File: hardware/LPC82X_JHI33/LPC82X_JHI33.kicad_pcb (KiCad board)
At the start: 2 copper layers, 23.6 x 23.5 mm, 24 parts, among them J1 Conn_02x09_Odd_Even, J2 Conn_02x09_Odd_Even, J3 JTAG_2X05, U1 LPC824M201JHI33, Y1 12MHz

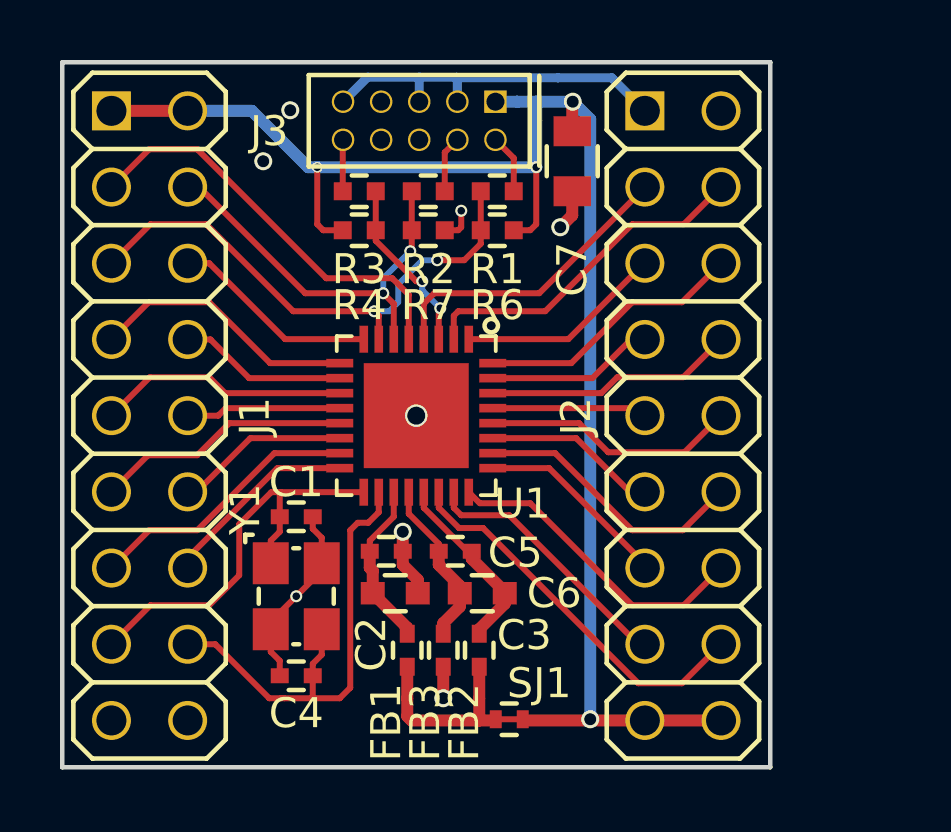
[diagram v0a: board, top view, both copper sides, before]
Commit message: LPC824 QFN33 new footprint for LPC and shrunk paste size
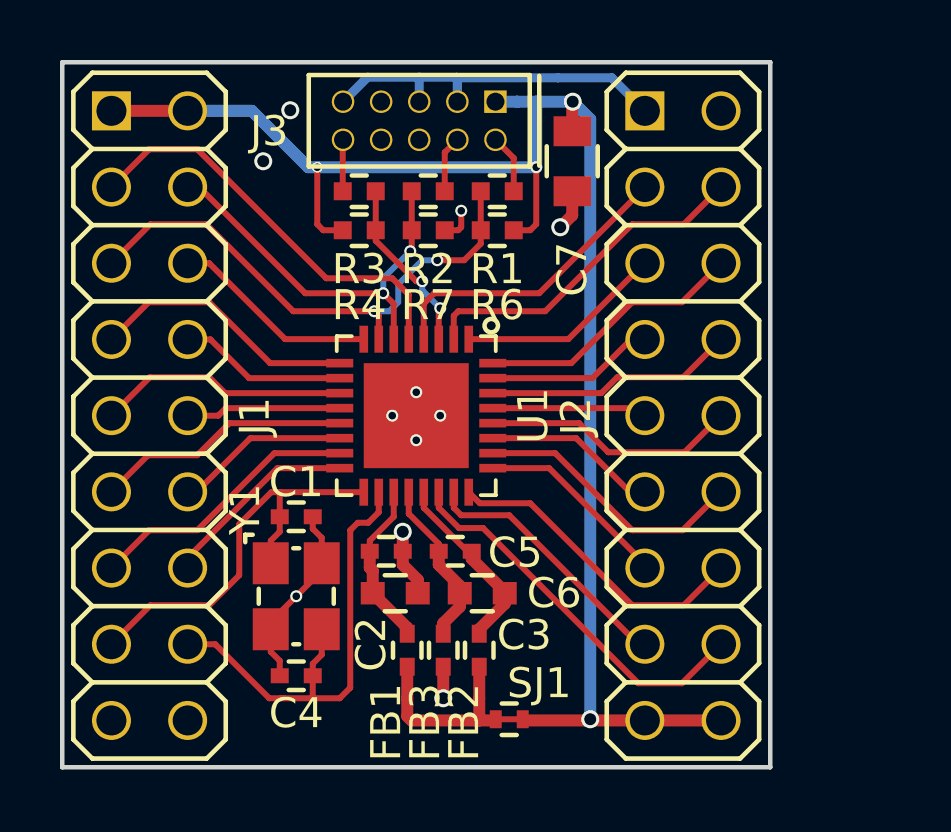
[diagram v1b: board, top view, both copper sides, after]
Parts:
- N2: value 20181124 -> 20190313
- U1: footprint SquantorIC:SOT617-3 -> SquantorIC:SOT617-3_alt_paste
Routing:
- net VSS: vias 8 -> 11
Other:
- rule solder_mask_min_width: 0.2 -> 0.1

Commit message: pcb net updates
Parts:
- N2: value 20190313 -> 20190411
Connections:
- net VDD renamed /VDD
- net VSS renamed /VSS

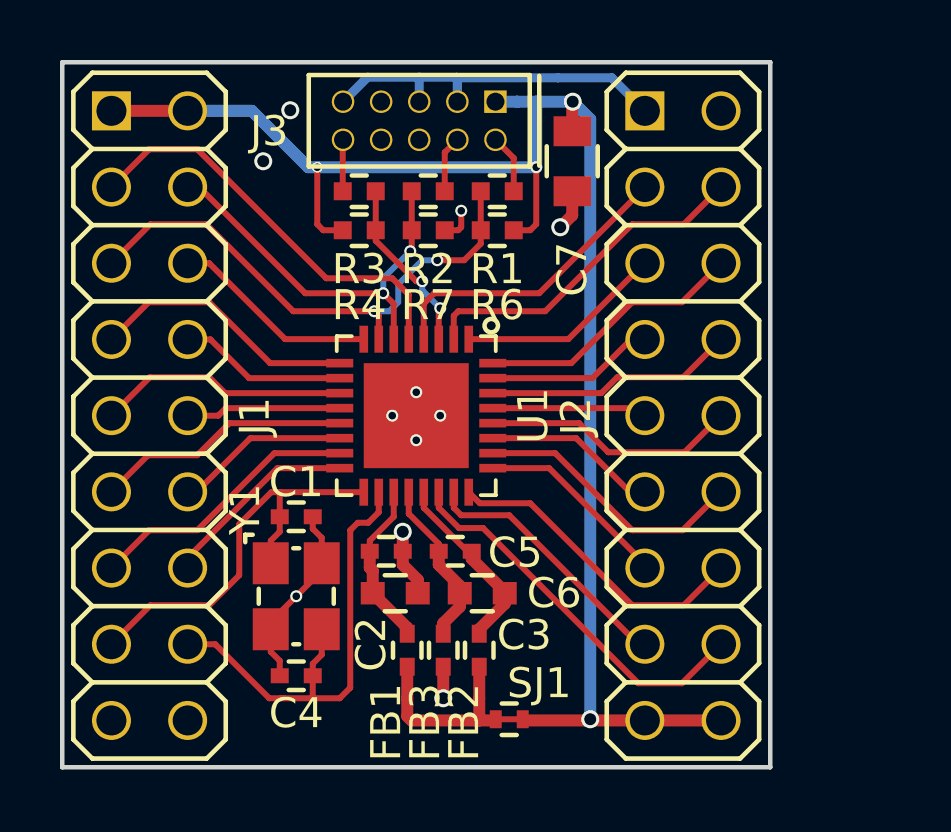
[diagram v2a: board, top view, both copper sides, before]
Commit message: changed connectors, newer component library
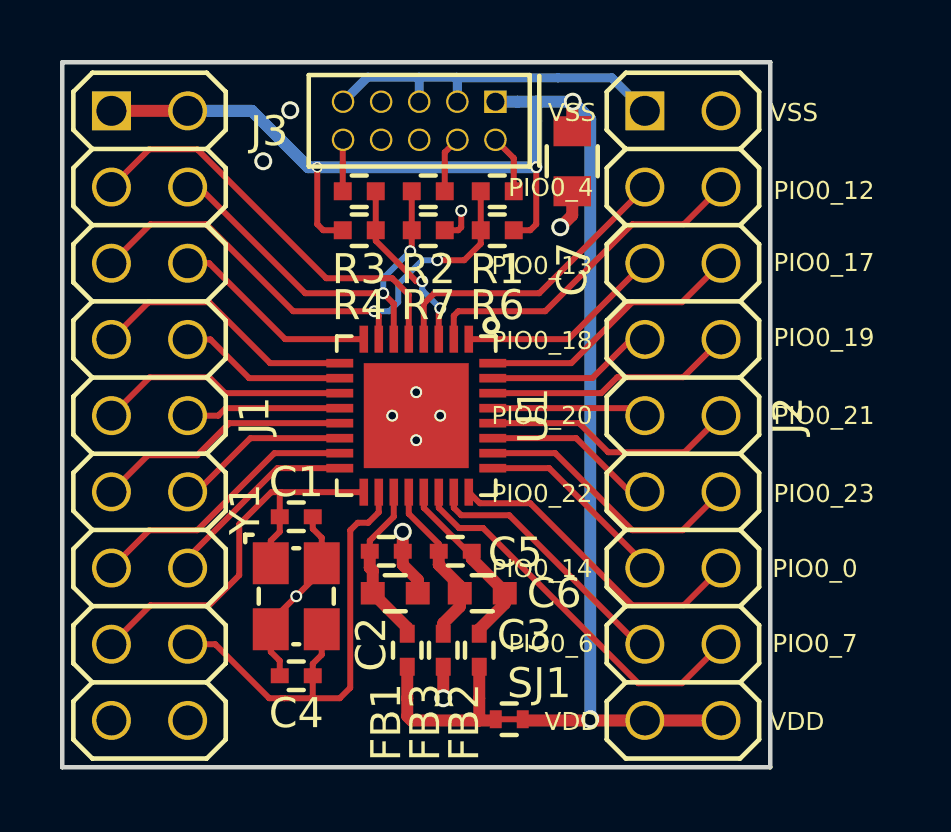
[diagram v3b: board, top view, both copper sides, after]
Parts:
- J1: value Conn_02x09_Odd_Even -> LPC82XJHI33_LEFT; footprint SquantorConnectors:Header-0254-2X09-H010 -> SquantorConnectorsNamed:LPC82XJHI33_breakout_left
- J2: value Conn_02x09_Odd_Even -> LPC82XJHI33_RIGHT; footprint SquantorConnectors:Header-0254-2X09-H010 -> SquantorConnectorsNamed:LPC82XJHI33_breakout_right
- moved N2 5.62 mm to (87.7, 110.7), turned to 180 degrees
- turned N1 to 180 degrees

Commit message: silk placement completed
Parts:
- moved N2 6.30 mm to (87.7, 117.0)
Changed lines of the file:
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@@
     (tags "LPC82XJHI33 breakout right")
     (attr virtual)
-    (fp_text reference J2 (at 0 -3.5 270) (layer F.SilkS)
+    (fp_text reference J2 (at 0.12 3.29 270) (layer F.SilkS)
       (effects (font (size 1 1) (thickness 0.15)))
     )
@@
       (effects (font (size 1 1) (thickness 0.15)))
     )
-    (fp_text user VSS (at -10.1 -3.7) (layer F.SilkS)
-      (effects (font (size 0.6 0.6) (thickness 0.12)))
-    )
-    (fp_text user PIO0_12 (at -7.5 -4.7) (layer F.SilkS)
-      (effects (font (size 0.6 0.6) (thickness 0.12)))
-    )
-    (fp_text user PIO0_17 (at -5.1 -4.7) (layer F.SilkS)
-      (effects (font (size 0.6 0.6) (thickness 0.12)))
-    )
-    (fp_text user PIO0_19 (at -2.6 -4.7) (layer F.SilkS)
-      (effects (font (size 0.6 0.6) (thickness 0.12)))
-    )
-    (fp_text user PIO0_21 (at 0 -4.7) (layer F.SilkS)
-      (effects (font (size 0.6 0.6) (thickness 0.12)))
-    )
-    (fp_text user PIO0_23 (at 2.6 -4.7) (layer F.SilkS)
-      (effects (font (size 0.6 0.6) (thickness 0.12)))
-    )
-    (fp_text user PIO0_0 (at 5.1 -4.4) (layer F.SilkS)
-      (effects (font (size 0.6 0.6) (thickness 0.12)))
-    )
-    (fp_text user PIO0_7 (at 7.6 -4.4) (layer F.SilkS)
-      (effects (font (size 0.6 0.6) (thickness 0.12)))
-    )
-    (fp_text user VDD (at 10.2 -3.8) (layer F.SilkS)
-      (effects (font (size 0.6 0.6) (thickness 0.12)))
-    )
-    (fp_text user VDD (at 10.2 3.7) (layer F.SilkS)
-      (effects (font (size 0.6 0.6) (thickness 0.12)))
-    )
-    (fp_text user PIO0_6 (at 7.6 4.4) (layer F.SilkS)
-      (effects (font (size 0.6 0.6) (thickness 0.12)))
-    )
-    (fp_text user PIO0_14 (at 5.1 4.7) (layer F.SilkS)
-      (effects (font (size 0.6 0.6) (thickness 0.12)))
-    )
-    (fp_text user PIO0_22 (at 2.6 4.7) (layer F.SilkS)
-      (effects (font (size 0.6 0.6) (thickness 0.12)))
-    )
-    (fp_text user PIO0_20 (at 0 4.7) (layer F.SilkS)
-      (effects (font (size 0.6 0.6) (thickness 0.12)))
-    )
-    (fp_text user PIO0_18 (at -2.5 4.7) (layer F.SilkS)
-      (effects (font (size 0.6 0.6) (thickness 0.12)))
-    )
-    (fp_text user PIO0_13 (at -5 4.7) (layer F.SilkS)
-      (effects (font (size 0.6 0.6) (thickness 0.12)))
-    )
-    (fp_text user PIO0_4 (at -7.6 4.4) (layer F.SilkS)
-      (effects (font (size 0.6 0.6) (thickness 0.12)))
-    )
-    (fp_text user VSS (at -10.1 3.7) (layer F.SilkS)
-      (effects (font (size 0.6 0.6) (thickness 0.12)))
+    (fp_text user PIO0_12 (at -6.28 4.19 180) (layer B.SilkS)
+      (effects (font (size 0.6 0.6) (thickness 0.12)) (justify mirror))
+    )
+    (fp_text user PIO0_17 (at -3.78 4.19 180) (layer B.SilkS)
+      (effects (font (size 0.6 0.6) (thickness 0.12)) (justify mirror))
+    )
+    (fp_text user PIO0_19 (at -1.28 4.19 180) (layer B.SilkS)
+      (effects (font (size 0.6 0.6) (thickness 0.12)) (justify mirror))
+    )
+    (fp_text user PIO0_21 (at 1.32 4.19 180) (layer B.SilkS)
+      (effects (font (size 0.6 0.6) (thickness 0.12)) (justify mirror))
+    )
+    (fp_text user PIO0_23 (at 3.82 4.19 180) (layer B.SilkS)
+      (effects (font (size 0.6 0.6) (thickness 0.12)) (justify mirror))
+    )
+    (fp_text user PIO0_0 (at 6.42 3.89 180) (layer B.SilkS)
+      (effects (font (size 0.6 0.6) (thickness 0.12)) (justify mirror))
+    )
+    (fp_text user PIO0_7 (at 8.92 3.89 180) (layer B.SilkS)
+      (effects (font (size 0.6 0.6) (thickness 0.12)) (justify mirror))
+    )
+    (fp_text user VDD (at 10.2 3.69 180) (layer B.SilkS)
+      (effects (font (size 0.6 0.6) (thickness 0.12)) (justify mirror))
+    )
+    (fp_text user PIO0_6 (at 7.6 4.4 180) (layer B.SilkS)
+      (effects (font (size 0.6 0.6) (thickness 0.12)) (justify mirror))
+    )
+    (fp_text user PIO0_14 (at 5.1 4.7 180) (layer B.SilkS)
+      (effects (font (size 0.6 0.6) (thickness 0.12)) (justify mirror))
+    )
+    (fp_text user PIO0_22 (at 2.6 4.7 180) (layer B.SilkS)
+      (effects (font (size 0.6 0.6) (thickness 0.12)) (justify mirror))
+    )
+    (fp_text user PIO0_20 (at -0.38 4.49 180) (layer B.SilkS)
+      (effects (font (size 0.6 0.6) (thickness 0.12)) (justify mirror))
+    )
+    (fp_text user PIO0_18 (at -2.5 4.7 180) (layer B.SilkS)
+      (effects (font (size 0.6 0.6) (thickness 0.12)) (justify mirror))
+    )
+    (fp_text user PIO0_13 (at -5 4.7 180) (layer B.SilkS)
+      (effects (font (size 0.6 0.6) (thickness 0.12)) (justify mirror))
+    )
+    (fp_text user PIO0_4 (at -7.6 4.4 180) (layer B.SilkS)
+      (effects (font (size 0.6 0.6) (thickness 0.12)) (justify mirror))
+    )
+    (fp_text user VSS (at -10.1 3.7 180) (layer B.SilkS)
+      (effects (font (size 0.6 0.6) (thickness 0.12)) (justify mirror))
     )
     (fp_line (start 9.525 2.54) (end 10.795 2.54) (layer F.SilkS) (width 0.1524))
@@
       (effects (font (size 0.6 0.6) (thickness 0.12)) (justify mirror))
     )
-    (fp_text user PIO0_26 (at 0 -4.7 180) (layer B.SilkS)
+    (fp_text user PIO0_26 (at -0.28 -4.49 180) (layer B.SilkS)
       (effects (font (size 0.6 0.6) (thickness 0.12)) (justify mirror))
     )
@@
       (effects (font (size 0.6 0.6) (thickness 0.12)) (justify mirror))
     )
-    (fp_text user VSS (at 10.2 -3.7 180) (layer B.SilkS)
+    (fp_text user VSS (at 10.22 -3.49 180) (layer B.SilkS)
       (effects (font (size 0.6 0.6) (thickness 0.12)) (justify mirror))
     )
@@
   )
   (module SquantorLabels:Label_version (layer B.Cu)
-    (at 87.7 110.7 180)
+    (at 87.7 117 180)
     (fp_text reference N2 (at 0 -1.4 180) (layer B.Fab) hide
       (effects (font (size 1 1) (thickness 0.15)) (justify mirror))
